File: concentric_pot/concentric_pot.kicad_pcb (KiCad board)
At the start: 2 copper layers, 19 x 18 mm, 2 parts, among them J1 Dual Pot

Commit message: Added fab and updates
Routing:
- net GND: vias 8 -> 7
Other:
- board text added: "GND"
- board text added: "MAX"
- board text added: "WIPER"
- board text removed: "IM"
- board text removed: "IW"
- board text removed: "OM"
- board text removed: "OW"
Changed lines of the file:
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@@
   (gr_arc (start 184 70) (mid 183.292893 69.707107) (end 183 69) (layer "Edge.Cuts") (width 0.2))
   (gr_arc (start 202 69) (mid 201.707107 69.707107) (end 201 70) (layer "Edge.Cuts") (width 0.2))
-  (gr_text "IM" (at 191.6 55.7) (layer "B.SilkS")
+  (gr_text "GND" (at 186.5 57 90) (layer "B.SilkS")
     (effects (font (size 0.5 0.5) (thickness 0.1)) (justify mirror))
   )
-  (gr_text "OM" (at 191.5 60.5) (layer "B.SilkS")
+  (gr_text "MAX" (at 189.1 57 90) (layer "B.SilkS")
     (effects (font (size 0.5 0.5) (thickness 0.1)) (justify mirror))
   )
-  (gr_text "IW" (at 186.5 55.7) (layer "B.SilkS")
-    (effects (font (size 0.5 0.5) (thickness 0.1)) (justify mirror))
-  )
-  (gr_text "OW" (at 186.4 60.5) (layer "B.SilkS")
+  (gr_text "WIPER" (at 184 57.000001 90) (layer "B.SilkS")
     (effects (font (size 0.5 0.5) (thickness 0.1)) (justify mirror))
   )
   (segment (start 192.5744 54.5744) (end 195 57) (width 0.4) (layer "B.Cu") (net 1))
   (segment (start 190.24 54.5744) (end 192.5744 54.5744) (width 0.4) (layer "B.Cu") (net 1))
-  (via (at 189.2 57) (size 0.8) (drill 0.4) (layers "F.Cu" "B.Cu") (net 2))
   (via (at 192.2 62.4) (size 0.8) (drill 0.4) (layers "F.Cu" "B.Cu") (net 2))
   (via (at 187.7 62.4) (size 0.8) (drill 0.4) (layers "F.Cu" "B.Cu") (net 2))

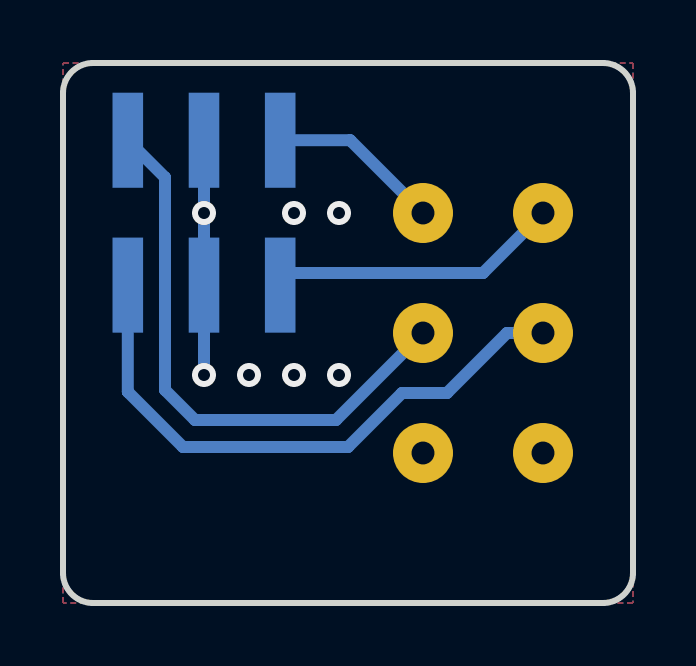
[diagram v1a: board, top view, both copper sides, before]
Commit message: Added taper resistor
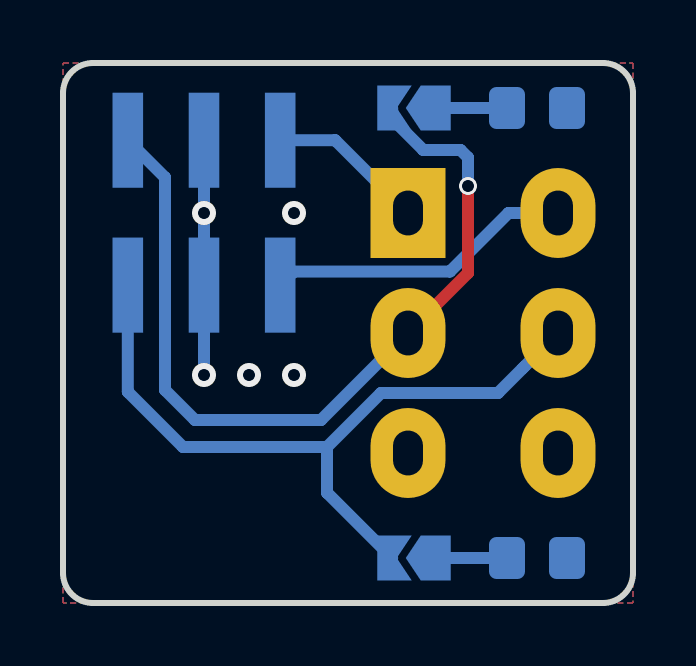
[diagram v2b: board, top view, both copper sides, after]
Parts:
- added JP1: SolderJumper_2_Open, Jumper:SolderJumper-2_P1.3mm_Open_TrianglePad1.0x1.5mm, B.Cu at (194.7, 53.5)
- added JP2: SolderJumper_2_Open, Jumper:SolderJumper-2_P1.3mm_Open_TrianglePad1.0x1.5mm, B.Cu at (194.7, 68.5)
- added R1: R_Small, Resistor_SMD:R_0805_2012Metric_Pad1.20x1.40mm_HandSolder, B.Cu at (198.8, 53.5)
- added R2: R_Small, Resistor_SMD:R_0805_2012Metric_Pad1.20x1.40mm_HandSolder, B.Cu at (198.8, 68.5)
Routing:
- net WIPER_INNER: track 19.1 -> 28.7 mm, vias 0 -> 1
- net WIPER_OUTER: track 19.7 -> 24.8 mm
- net Net-(R2-Pad2): track 0.00 -> 2.38 mm
- net Net-(R1-Pad2): track 0.00 -> 2.38 mm
- net MAX_INNER: track 5.76 -> 5.26 mm
- net GND: vias 7 -> 5
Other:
- board text added: "EXP"
